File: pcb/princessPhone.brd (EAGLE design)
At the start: 63.5 x 100 mm, 48 parts, among them IC1 OPA2134UA, P2 TC2030-MCP-NL, Q1 BF245, U1 AG1170-S3, U2 PIC32MX170D, U3 BLUETOOTH-RN-52, U4 V_REG_LD1085D2, X1 22-23-2041, X3 USB_MICRO_B

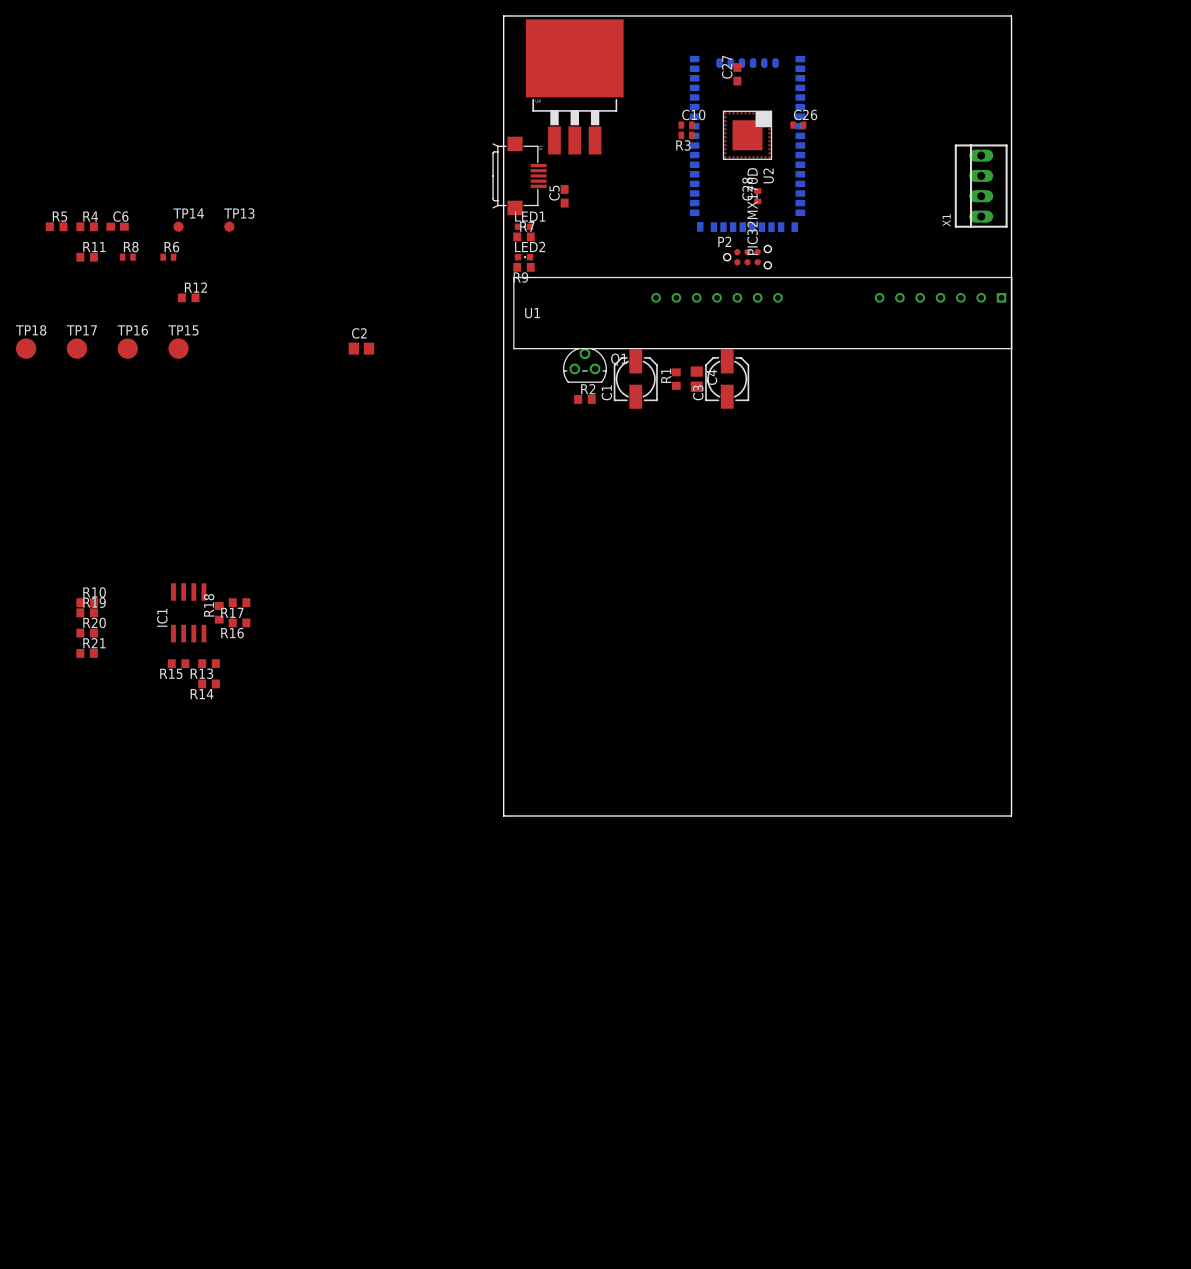
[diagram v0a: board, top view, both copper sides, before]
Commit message: -Changed MCU package -Added RJ-11 connector
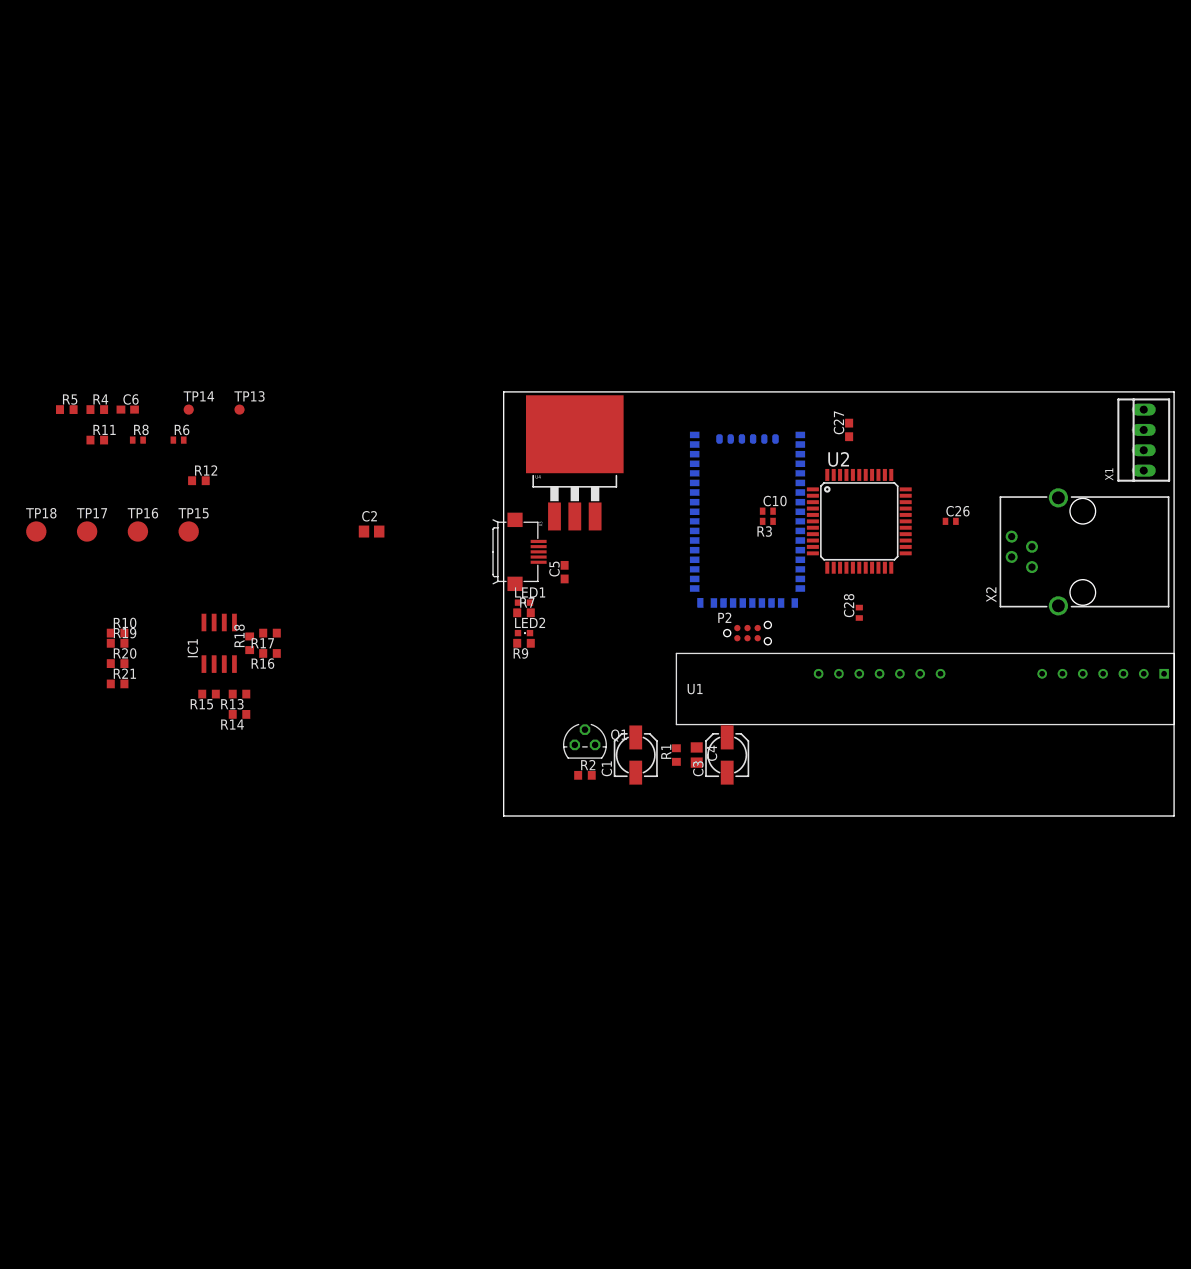
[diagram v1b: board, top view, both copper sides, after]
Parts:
- added X2: XRJK-S-01-6-4-0-9M2, con-xmultiple:XRJK-S-01-6-4-0-9M2
- U1: value AG1170-S3 -> AG1170-S3-VERTICAL
- U2: value PIC32MX170D -> PI32MX170D-PT; device raveGear5:VTLA44 -> raveGear5:TQFP44
- moved C28 53.6 mm to (44.5, 25.4)
- moved C26 53.1 mm to (55.9, 36.8)
- moved U1 51.2 mm to (61.0, 17.8)
- moved U2 50.2 mm to (44.5, 36.8), turned to 0 degrees
- moved R3 49.3 mm to (33.0, 36.8)
- moved C10 49.3 mm to (33.0, 38.1)
- moved C1 47.0 mm to (16.5, 7.62)
- moved C3 47.0 mm to (27.9, 7.62)
- moved C4 47.0 mm to (24.1, 7.62)
- moved Q1 47.0 mm to (10.2, 8.89)
- moved R1 47.0 mm to (21.6, 7.62)
- moved R2 47.0 mm to (10.2, 5.08)
- moved R7 47.0 mm to (2.54, 25.4)
- moved U3 47.0 mm to (30.5, 38.1)
- moved X3 47.0 mm to (1.27, 33.0)
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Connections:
- removed net +2V5: P2.6
- removed net RING: U1.1, X1.1
- removed net TIP: U1.2, X1.2
- new net PHONE_RING: U1.1, X1.1, X2.2
- new net PHONE_TIP: U1.2, X1.2, X2.3
- net GND: no longer U2.45
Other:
- board size 63.5 x 100 mm -> 83.8 x 53 mm

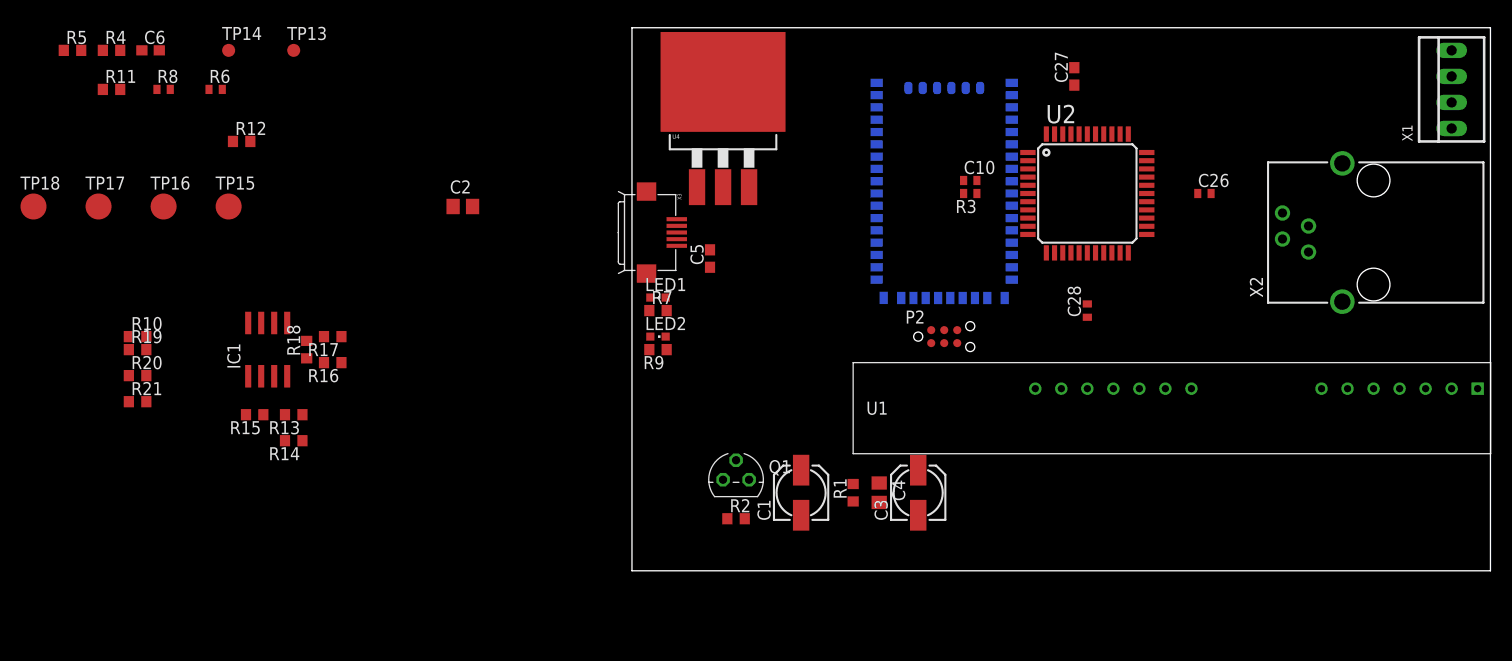
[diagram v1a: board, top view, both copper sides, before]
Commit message: -Added to library -Added line-level components -Cleaned up schematic
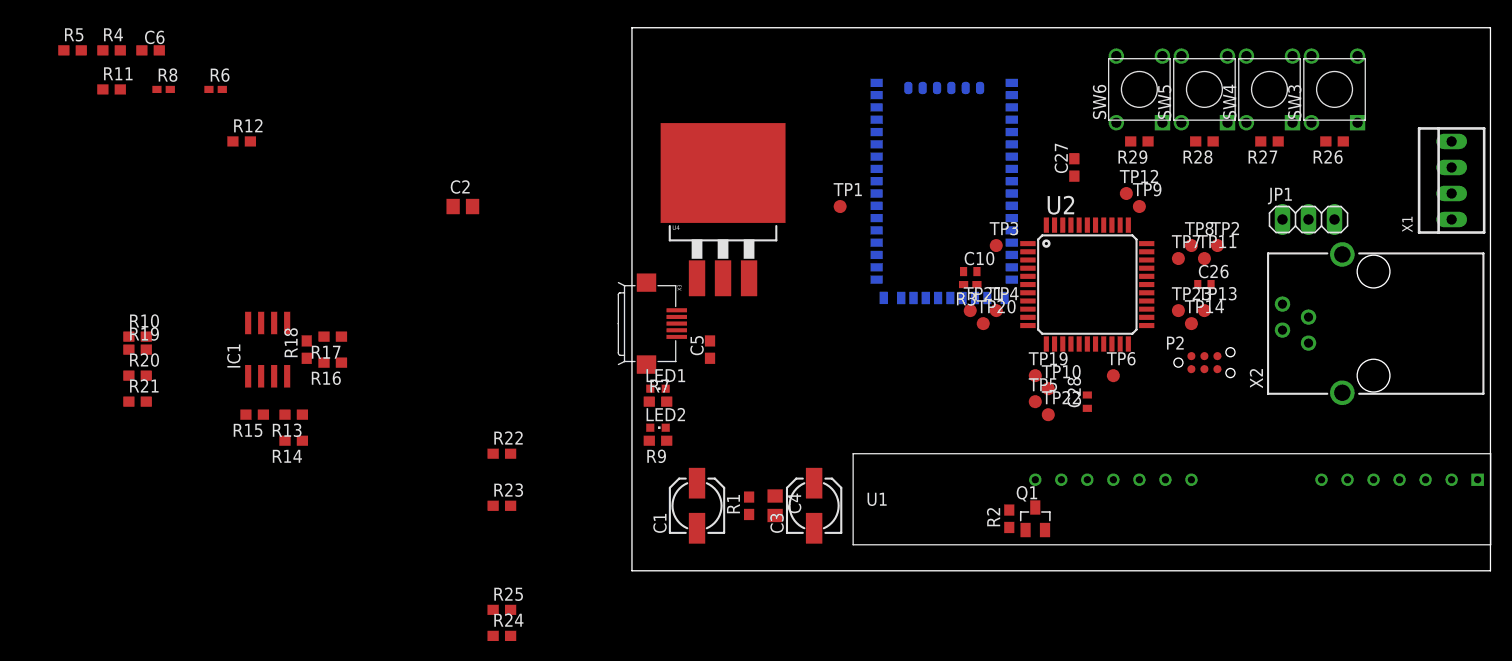
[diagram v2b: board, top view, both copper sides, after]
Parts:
- removed TP15, TP16, TP17, TP18: PTR1B2,54, testpad:B2,54
- added JP1: (no value), pinhead:1X03
- added R22, R26, R27, R28, R29: 10K, rcl:R0603
- added R23: 1K, rcl:R0603
- added R24, R25: 0, rcl:R0603
- added SW3, SW4, SW5, SW6: LL1105BF250Q, raveGearControl:LL1105
- added TP1, TP10, TP11, TP12, TP19, TP2, TP20, TP21, TP22, TP23, TP3, TP4, TP5, TP6, TP7, TP8, TP9: PTR1B1,27, testpad:B1,27
- Q1: value BF245 -> 2N7002K; device transistor-fet:TO92 -> princessPhone:SOT23
- R10, R19, R20, R21: value 0 -> NP
- R12: value 22K -> NP
- R13, R14: value 47 -> NP
- moved TP14 97.7 mm to (54.6, 24.1)
- moved TP13 92.5 mm to (55.9, 25.4)
- moved Q1 29.5 mm to (39.4, 5.08)
- moved R2 26.7 mm to (36.8, 5.08), turned to 90 degrees
- moved P2 25.5 mm to (53.3, 20.3)
- moved C1 10.2 mm to (6.35, 6.35)
- moved C3 10.2 mm to (17.8, 6.35)
- moved R1 10.2 mm to (11.4, 6.35)
- moved C4 10.2 mm to (14.0, 6.35)
- moved X2 8.89 mm to (72.4, 24.1)
- moved X3 8.89 mm to (1.27, 24.1)
- moved C10 8.89 mm to (33.0, 29.2)
- moved C27 8.89 mm to (43.2, 39.4)
- moved C5 8.89 mm to (7.62, 21.6)
- moved LED1 8.89 mm to (2.54, 17.8)
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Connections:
- net N$5 renamed LED0
- net N$7 renamed LED1
- removed net FPGA_SPI_SS: U2.43
- removed net N$6: X1.4
- removed net PIC32_MISO: U2.44
- removed net PIC32_MOSI: U2.41
- removed net PIC32_SCK: U2.14
- removed net ROTARY: X1.3
- removed net VCC: P2.2
- new net AG1170_AUDIO_IN_AGG: R22.1, R23.2
- new net N$11: TP1.TP, U3.31
- new net PIC32_RSVD_1: TP6.TP, U2.19
- new net PIC32_RSVD_10: TP3.TP, U2.1
- new net PIC32_RSVD_11: TP4.TP, U2.9
- new net PIC32_RSVD_12: TP5.TP, U2.14
- new net PIC32_RSVD_2: TP7.TP, U2.30
- new net PIC32_RSVD_3: TP8.TP, U2.31
- new net PIC32_RSVD_4: TP9.TP, U2.34
- new net PIC32_RSVD_5: TP10.TP, U2.13
- new net PIC32_RSVD_6: TP11.TP, U2.32
- new net PIC32_RSVD_7: TP12.TP, U2.35
- new net PIC32_RSVD_8: TP19.TP, U2.12
- new net PIC32_RSVD_9: TP2.TP, U2.33
- new net SW0: R26.2, SW3.3, U2.41
- new net SW1: R27.2, SW4.3, U2.42
- new net SW2: R28.2, SW5.3, U2.43
- new net SW3: R29.2, SW6.3, U2.44
- net +3V3: now also P2.2, R26.1, R27.1, R28.1, R29.1
- net AG1170_AUDIO_OUT: now also R24.2, R25.2
- net GND: now also JP1.1, R23.1, SW3.1, SW4.1, SW5.1, SW6.1; no longer TP18.TP
- net N$2: now also Q1.1; no longer Q1.3
- net N$3: now also Q1.3; no longer Q1.1
- net PIC32_U1RX_3V3: now also JP1.2
- net PIC32_U1TX_3V3: now also JP1.3
- net RN52_MIC_L+: now also R24.1, R25.1
- net RN52_SPKR_L+: now also R22.2
- net SST25_CE#: now also TP20.TP
- net SST25_MISO: now also TP23.TP
- net SST25_MOSI: now also TP21.TP
- net SST25_SCK: now also TP22.TP
- net USB_DM: no longer TP16.TP
- net USB_DP: no longer TP17.TP
- net USB_VBUS: no longer TP15.TP
